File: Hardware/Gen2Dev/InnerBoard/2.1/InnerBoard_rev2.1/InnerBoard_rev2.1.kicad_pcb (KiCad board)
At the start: 2 copper layers, 101.6 x 76.2 mm, 177 parts, among them J1 HMTSW-102-X-X-S-X, J10 HMTSW-102-X-X-S-X, J11 HMTSW-102-X-X-S-X, J12 HMTSW-102-X-X-S-X, J13 HMTSW-102-X-X-S-X, J14 HMTSW-102-X-X-S-X, J15 HMTSW-102-X-X-S-X, J16 HMTSW-102-X-X-S-X, J17 HMTSW-102-X-X-S-X, J18 HMTSW-102-X-X-S-X, J19 HMTSW-102-X-X-S-X, J2 HMTSW-102-X-X-S-X, J3 HMTSW-102-X-X-S-X, J4 HMTSW-102-X-X-S-X, J5 UJ31-CH-G2-SMT-TR, J6 SI-46020-F, J7 HMTSW-102-X-X-S-X, J8 3221-10-0300-00, J9 HMTSW-102-X-X-S-X, Q1 SI2323DS-T1-GE3, Q10 BSS138, Q4 BC817, Q5 BC817, Q9 SI2323DS-T1-GE3, SW1 PTS815 SJM 250 SMTR LFS, SW2 PTS815 SJM 250 SMTR LFS, U1 LM5156DSSR, U10 ESP32-WROOM-32E-N8, U11 LAN8710A-EZC, U12 TPS2376PW, U13 RFM-0505S, U16 ROE-0512S, U23 ESDS314DBVR, U4 MIC5504-3.3YM5, U6 74LVC1G04, U7 LD1117S50TR_SOT223, U9 FT232RQ, Y1 ABLS2-12.000MHZ-D4Y-T, Y3 ASV-50.000MHZ-LCS-T

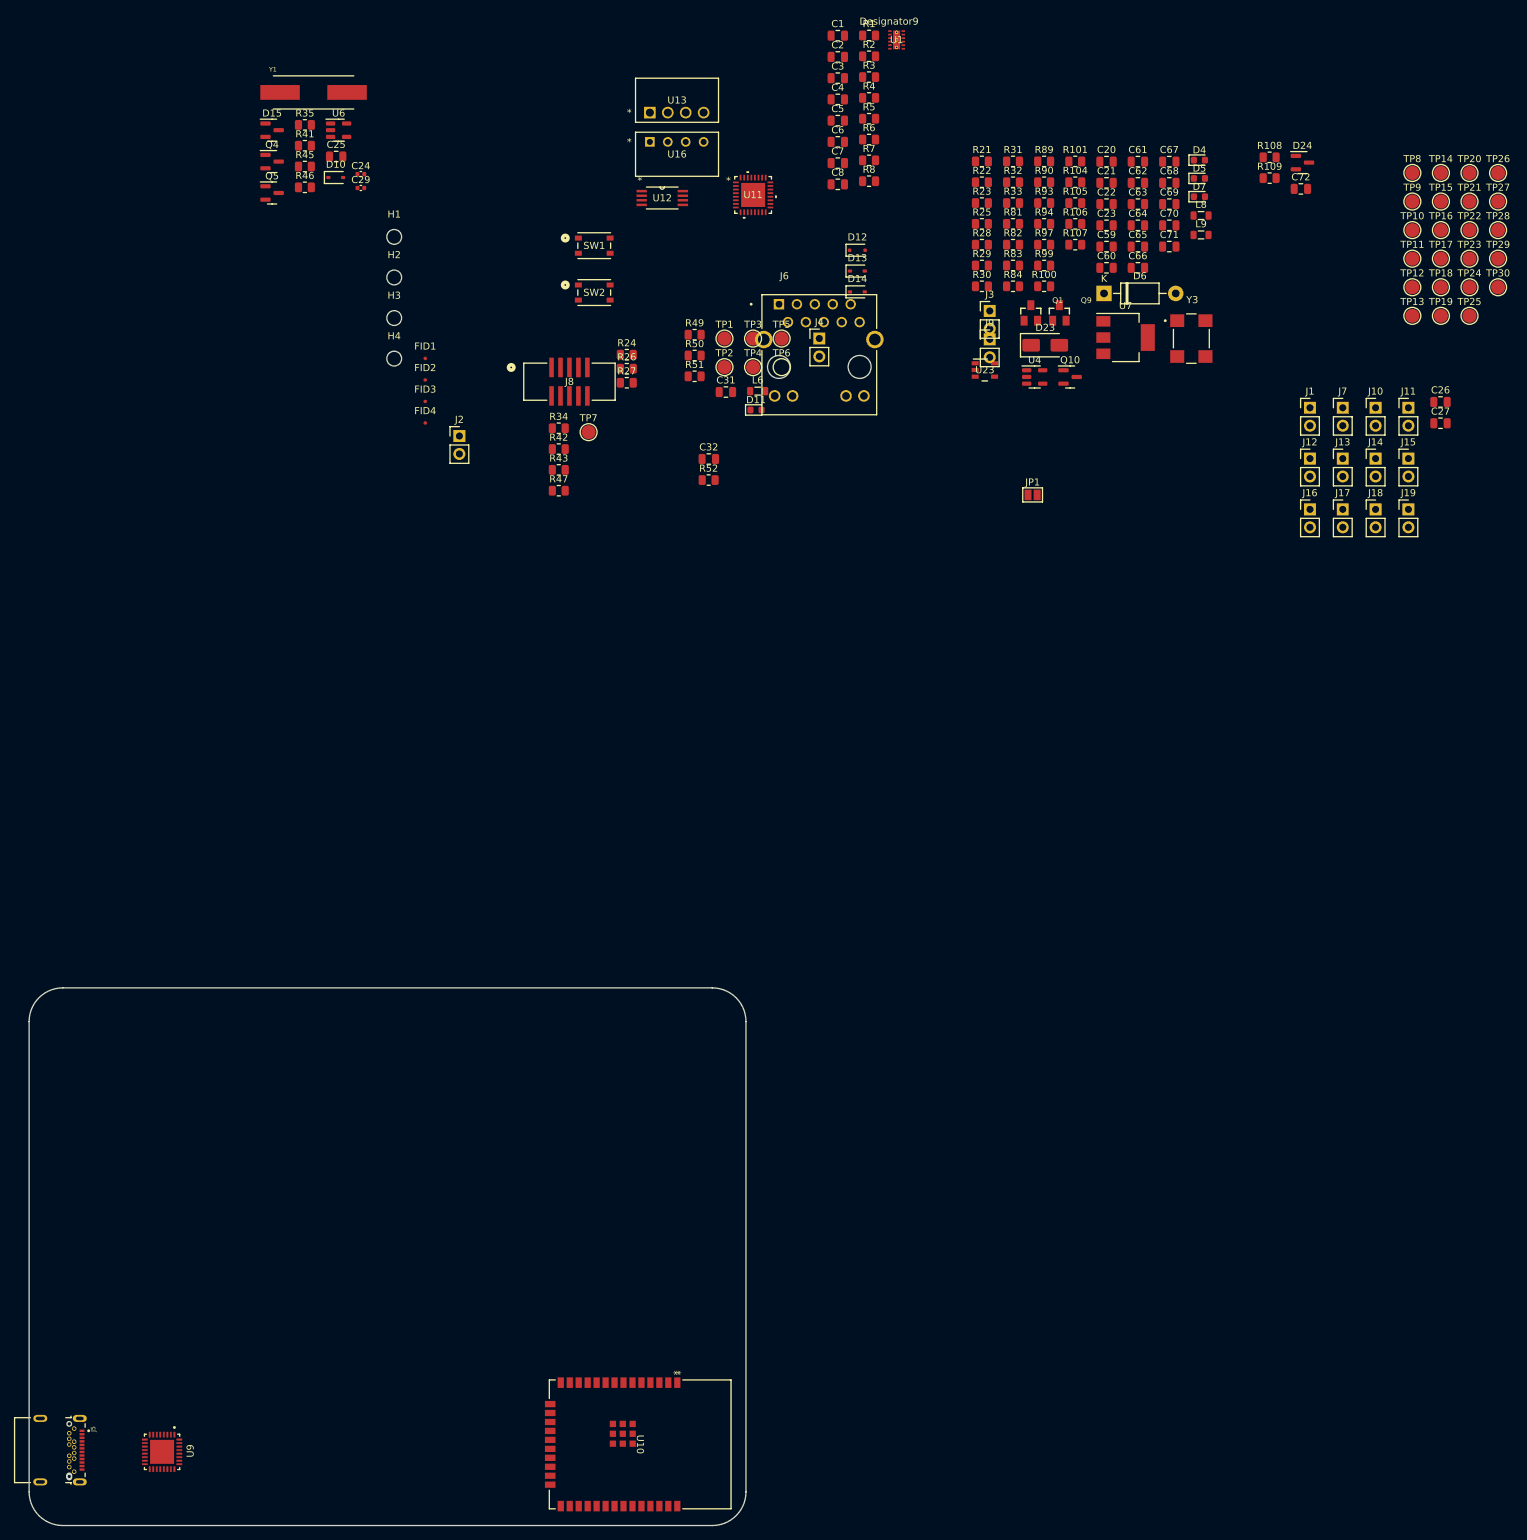
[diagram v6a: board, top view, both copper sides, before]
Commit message: Inner board 2.1 footprint links refactored (for future work) and added all links. Routing progress
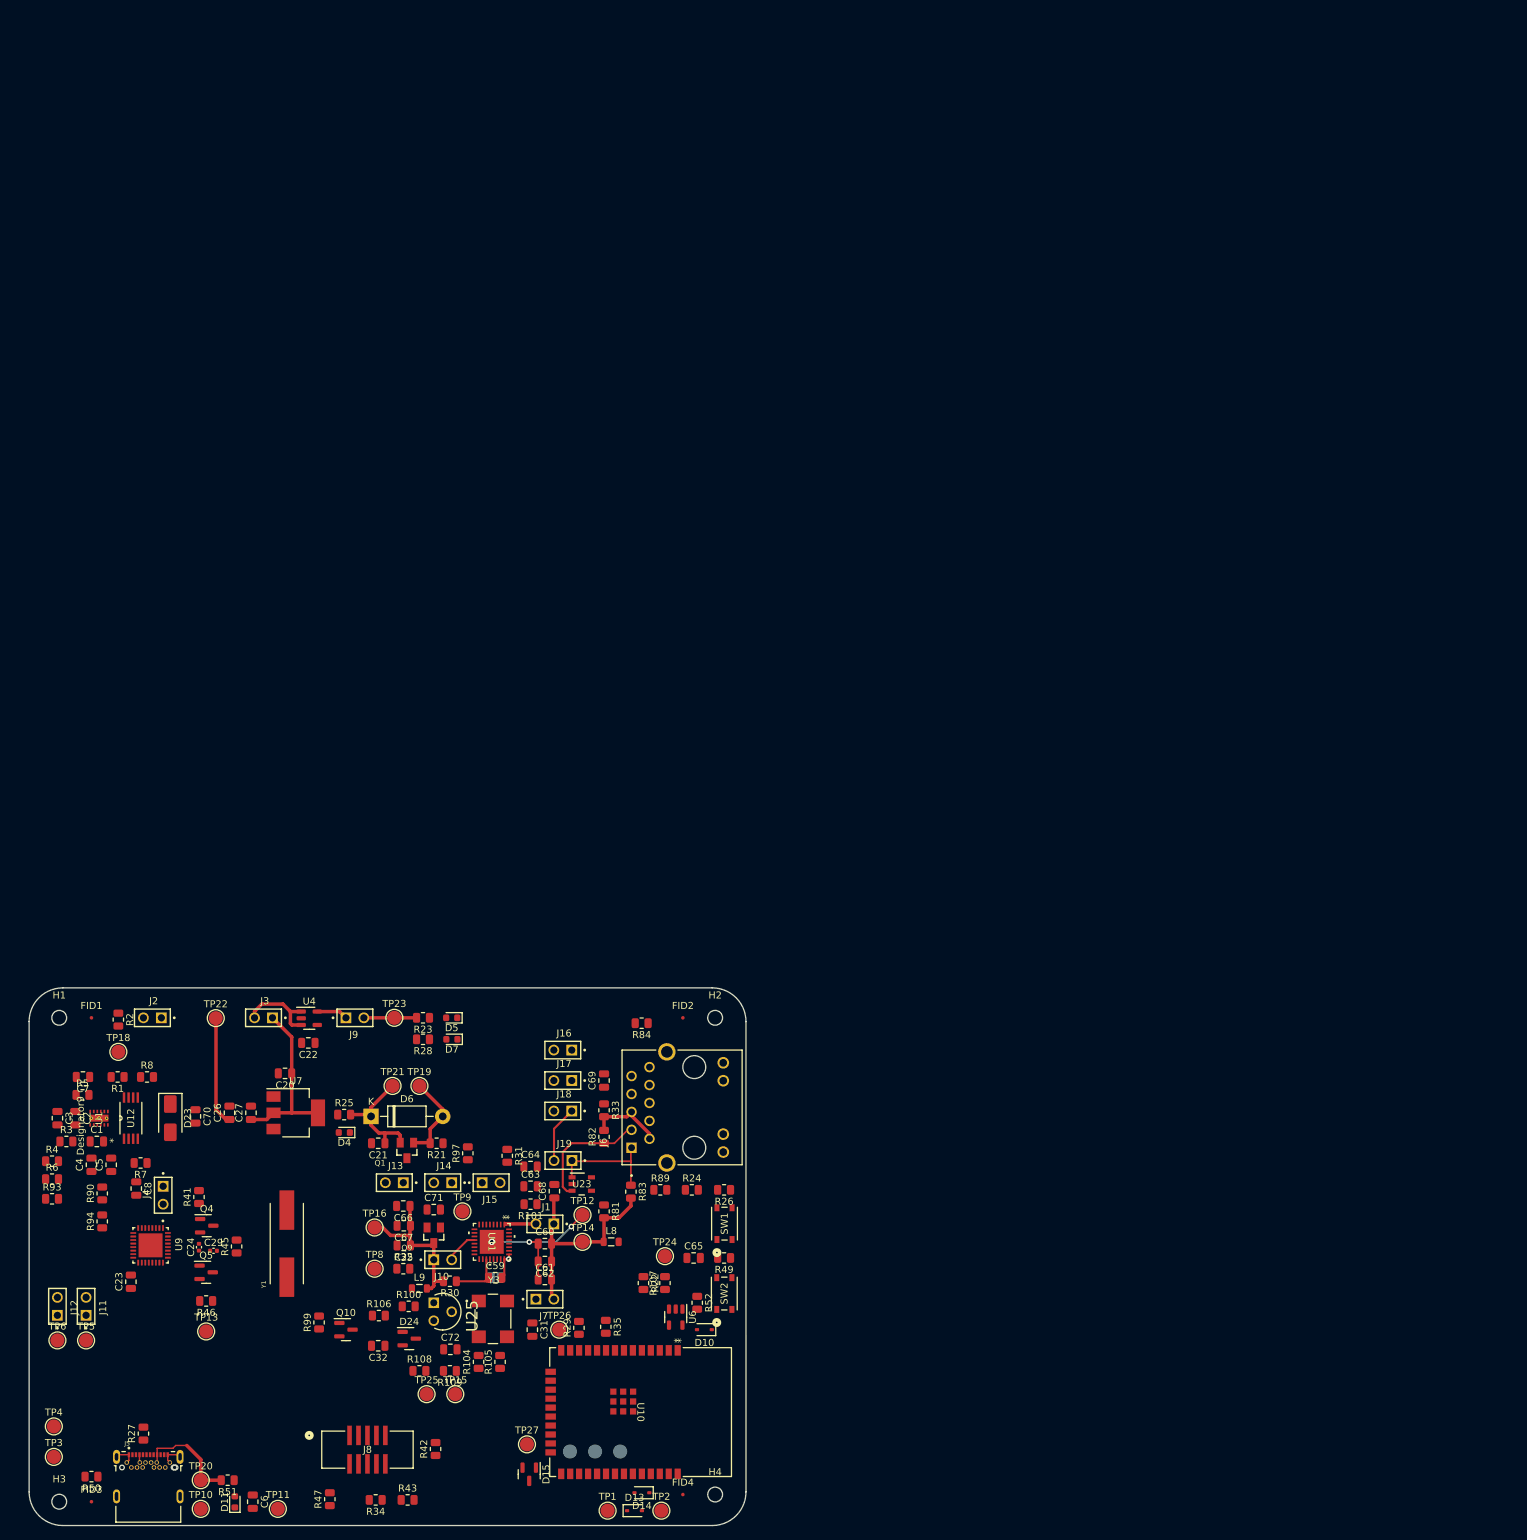
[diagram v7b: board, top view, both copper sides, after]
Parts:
- removed D12: PMEG6010CEJ, Diode_SMD:D_SOD-323F
- removed L6: FB0805/600R/2A, Inductor_SMD:L_0805_2012Metric
- removed TP17, TP7: TestPoint, TestPoint:TestPoint_Pad_D2.0mm
- removed U13: RFM-0505S, RFM_0505S:SIP4_RFM_RCP
- removed U16: ROE-0512S, ROE-0512S:ROE_RCP
- added U25: MCP100-270D, MCP100-270D:TO127P254X495-3, F.Cu at (149.6, 106.4)
- J1, J10, J11, J12, J13, J14, J15, J16, J17, J18, J19, J2, J3, J4, J7, J9: footprint Connector_PinHeader_2.54mm:PinHeader_1x02_P2.54mm_Vertical -> HMTSW-102-X-X-S-X:SAMTEC_HMTSW-102-X-X-S-X
- J8: footprint 3221-10-0300-00:CONN10_3221-10-0300-00_CNC -> CONN10_3221-10-0300-00_CNC:CONN10_3221-10-0300-00_CNC
- JP1, TP28, TP29, TP30: moved to B.Cu
- U11: footprint LAN8710A_EZC:QFN32_5X5MC_MCH -> LAN8710A-EZC:QFN32_5X5MC_MCH
- moved TP20 258.2 mm to (114.0, 129.0)
- moved TP10 249.7 mm to (114.0, 133.1)
- moved TP11 239.3 mm to (125.0, 133.1)
- moved J11 226.6 mm to (97.8, 104.4), turned to -90 degrees
- moved TP27 223.5 mm to (160.3, 124.0)
- moved TP13 223.5 mm to (114.8, 108.0)
- moved TP15 219.3 mm to (150.1, 116.8)
- moved TP28 217.4 mm to (166.4, 125.0), turned to 180 degrees
- moved TP18 216.5 mm to (102.4, 68.3)
- moved J12 214.4 mm to (93.7, 104.4), turned to -90 degrees
- moved TP8 213.9 mm to (138.7, 99.1)
- moved TP25 212.6 mm to (146.1, 116.8)
- moved TP29 212.0 mm to (169.9, 125.0), turned to 180 degrees
- moved TP26 211.1 mm to (164.8, 107.7)
- moved R108 210.0 mm to (145.0, 113.5)
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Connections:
- U11 pad 1: VDDA1/2 -> Net-(U11-VDD2A)
- U11 pad 12: +3.3VLAN -> Net-(U11-VDDIO)
- U11 pad 27: VDDA1/2 -> Net-(U11-VDD1A)
- U11 pad 29: Net-(J6-TD+) -> Net-(U11-TXP)
- U11 pad 30: Net-(J6-RD-) -> Net-(U11-RXN)
- U11 pad 31: Net-(J6-RD+) -> Net-(U11-RXP)
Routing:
- net VDDA1/2: track 0.00 -> 42.2 mm
- net +5V: track 0.00 -> 41.6 mm
- net +3.3VLAN: track 0.00 -> 23.2 mm
- net Net-(U11-EPAD): track 0.00 -> 20.9 mm, vias 0 -> 7
- net Net-(J6-TD-): track 0.00 -> 17.6 mm
- net VBUS: track 0.00 -> 16.2 mm
- net Net-(J6-TD+): track 0.00 -> 16.0 mm
- net +9V: track 0.00 -> 15.5 mm
- net +5VP: track 0.00 -> 12.6 mm
- net Net-(U4-EN): track 0.00 -> 11.7 mm
- net Spare2: track 0.00 -> 10.3 mm, vias 0 -> 1
- net Net-(J18-Pad01): track 0.00 -> 8.06 mm
- net Net-(JP1-B): track 0.00 -> 7.52 mm
- net +3.3V: track 0.00 -> 7.47 mm
- net Net-(U11-VDDIO): track 0.00 -> 4.72 mm
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- added copper zone on In1.Cu, net Spare2
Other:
- copper layers 2 -> 4

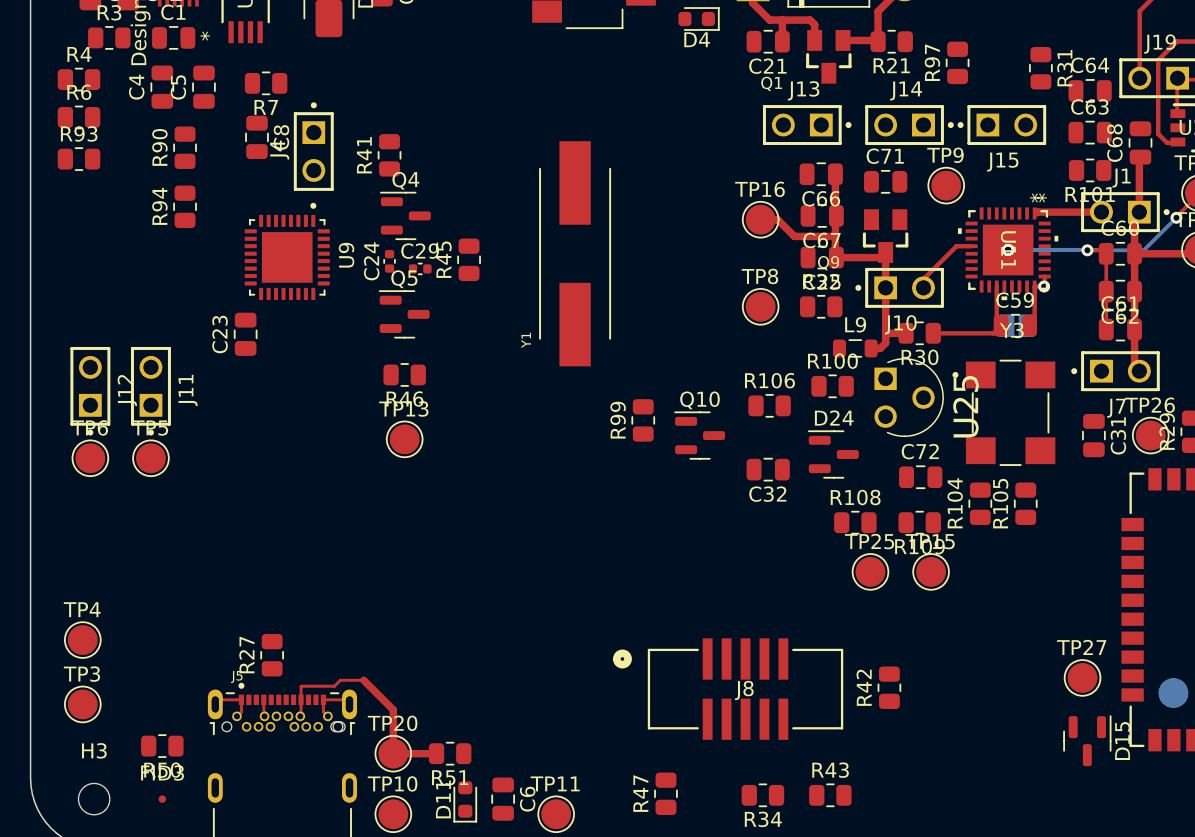
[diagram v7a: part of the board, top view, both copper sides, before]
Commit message: Routing progress. Mergedf 3.3v and 3v3
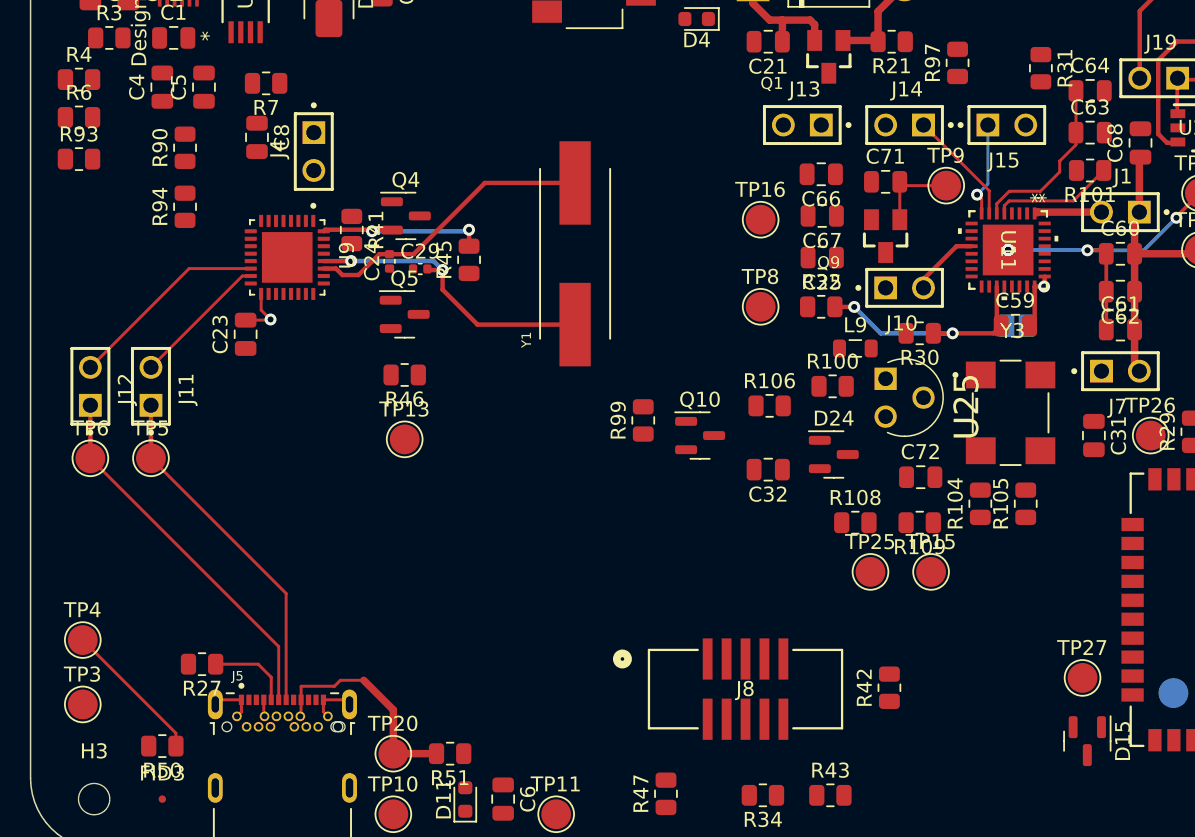
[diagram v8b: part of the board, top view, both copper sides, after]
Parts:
- moved R41 5.61 mm to (111.3, 93.9), turned to -90 degrees
- moved R27 4.74 mm to (101.2, 123.0), turned to 180 degrees
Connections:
- J8 pad 10: +3V3 -> +3.3V
- R26 pad 1: +3V3 -> +3.3V
- R34 pad 1: +3V3 -> +3.3V
- R42 pad 1: +3V3 -> +3.3V
- R43 pad 1: +3V3 -> +3.3V
- R47 pad 1: +3V3 -> +3.3V
- R52 pad 1: +3V3 -> +3.3V
- U10 pad 2: +3V3 -> +3.3V
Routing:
- net USB_DP: track 0.00 -> 25.0 mm
- net USB_DN: track 0.00 -> 23.5 mm
- net +3.3VLAN: track 23.2 -> 0.00 mm
- net Net-(U9-OSCO): track 0.00 -> 20.4 mm, vias 0 -> 2
- net Net-(U9-OSCI): track 0.00 -> 19.6 mm
- net Net-(U9-USBDP): track 0.00 -> 13.5 mm
- net Net-(Q4-E): track 0.00 -> 12.2 mm, vias 0 -> 2
- net Net-(U11-VDDCR): track 0.00 -> 11.6 mm
- net Net-(J5-CC2): track 0.00 -> 9.70 mm
- net Net-(U9-USBDM): track 0.00 -> 9.23 mm
- net Net-(JP1-B): track 7.52 -> 16.2 mm, vias 0 -> 2
- net GPIO0/XTAL1/CLKIN: track 0.00 -> 8.16 mm
- net PHYAD1: track 0.00 -> 7.76 mm
- net PHYAD2: track 0.00 -> 6.36 mm, vias 0 -> 1
- net Net-(C71-Pad2): track 0.00 -> 5.76 mm
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- added copper zone on In2.Cu, net +3.3V
